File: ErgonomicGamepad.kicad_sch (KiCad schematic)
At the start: 86 parts, among them J1 USB_C_Receptacle_USB2.0_16P, J2 Conn_01x05, J3 Conn_01x05, J4 Conn_01x05, J5 AVR-ISP-6, J6 Conn_01x05, J7 1824417, SW01 SW_DIP_x01, SW02 SW_DIP_x01, SW03 SW_DIP_x01, SW04 SW_DIP_x01, SW05 SW_DIP_x01, SW06 SW_DIP_x01, SW07 SW_DIP_x01, SW08 SW_DIP_x01, SW09 SW_DIP_x01, SW10 SW_DIP_x01, SW11 SW_DIP_x01, SW12 SW_DIP_x01, SW13 SW_DIP_x01, SW14 SW_DIP_x01, SW15 SW_DIP_x01, SW16 SW_DIP_x01, SW17 SW_DIP_x01, SW18 SW_DIP_x01, SW19 SW_DIP_x01, SW20 SW_DIP_x01, SW21 SW_DIP_x01, SW22 SW_DIP_x01, SW23 SW_DIP_x01, SW24 SW_DIP_x01, U1 ATmega32U4-A, U2 USBLC6-2SC6, Y1 Crystal

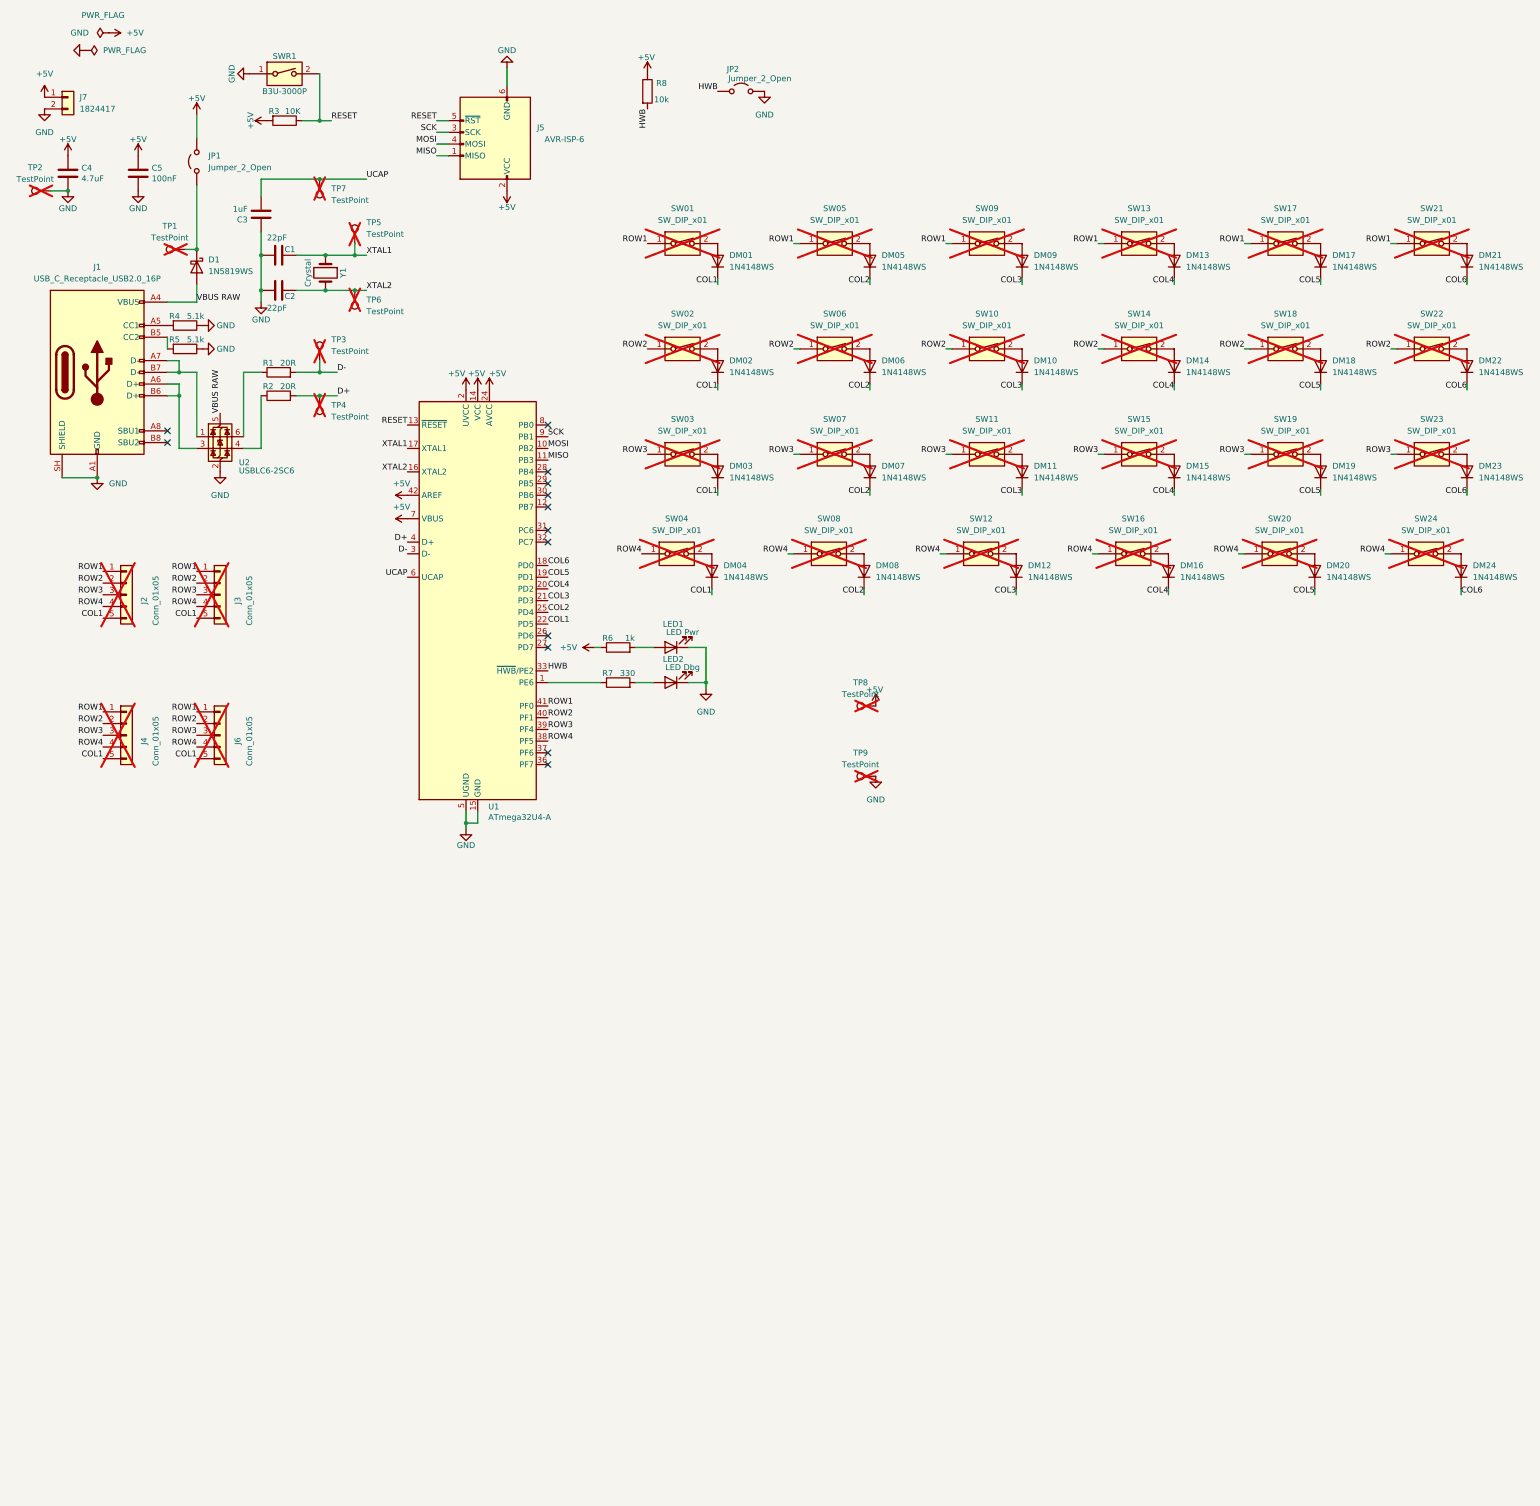
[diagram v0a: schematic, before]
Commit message: Split key matrix into Pinkie/Thumb satellite hierarchical sheets
Move satellite switches off the main schematic into their own sheets
and promote the crossing ROW/COL matrix nets to global labels so
connectivity survives the sheet boundary.
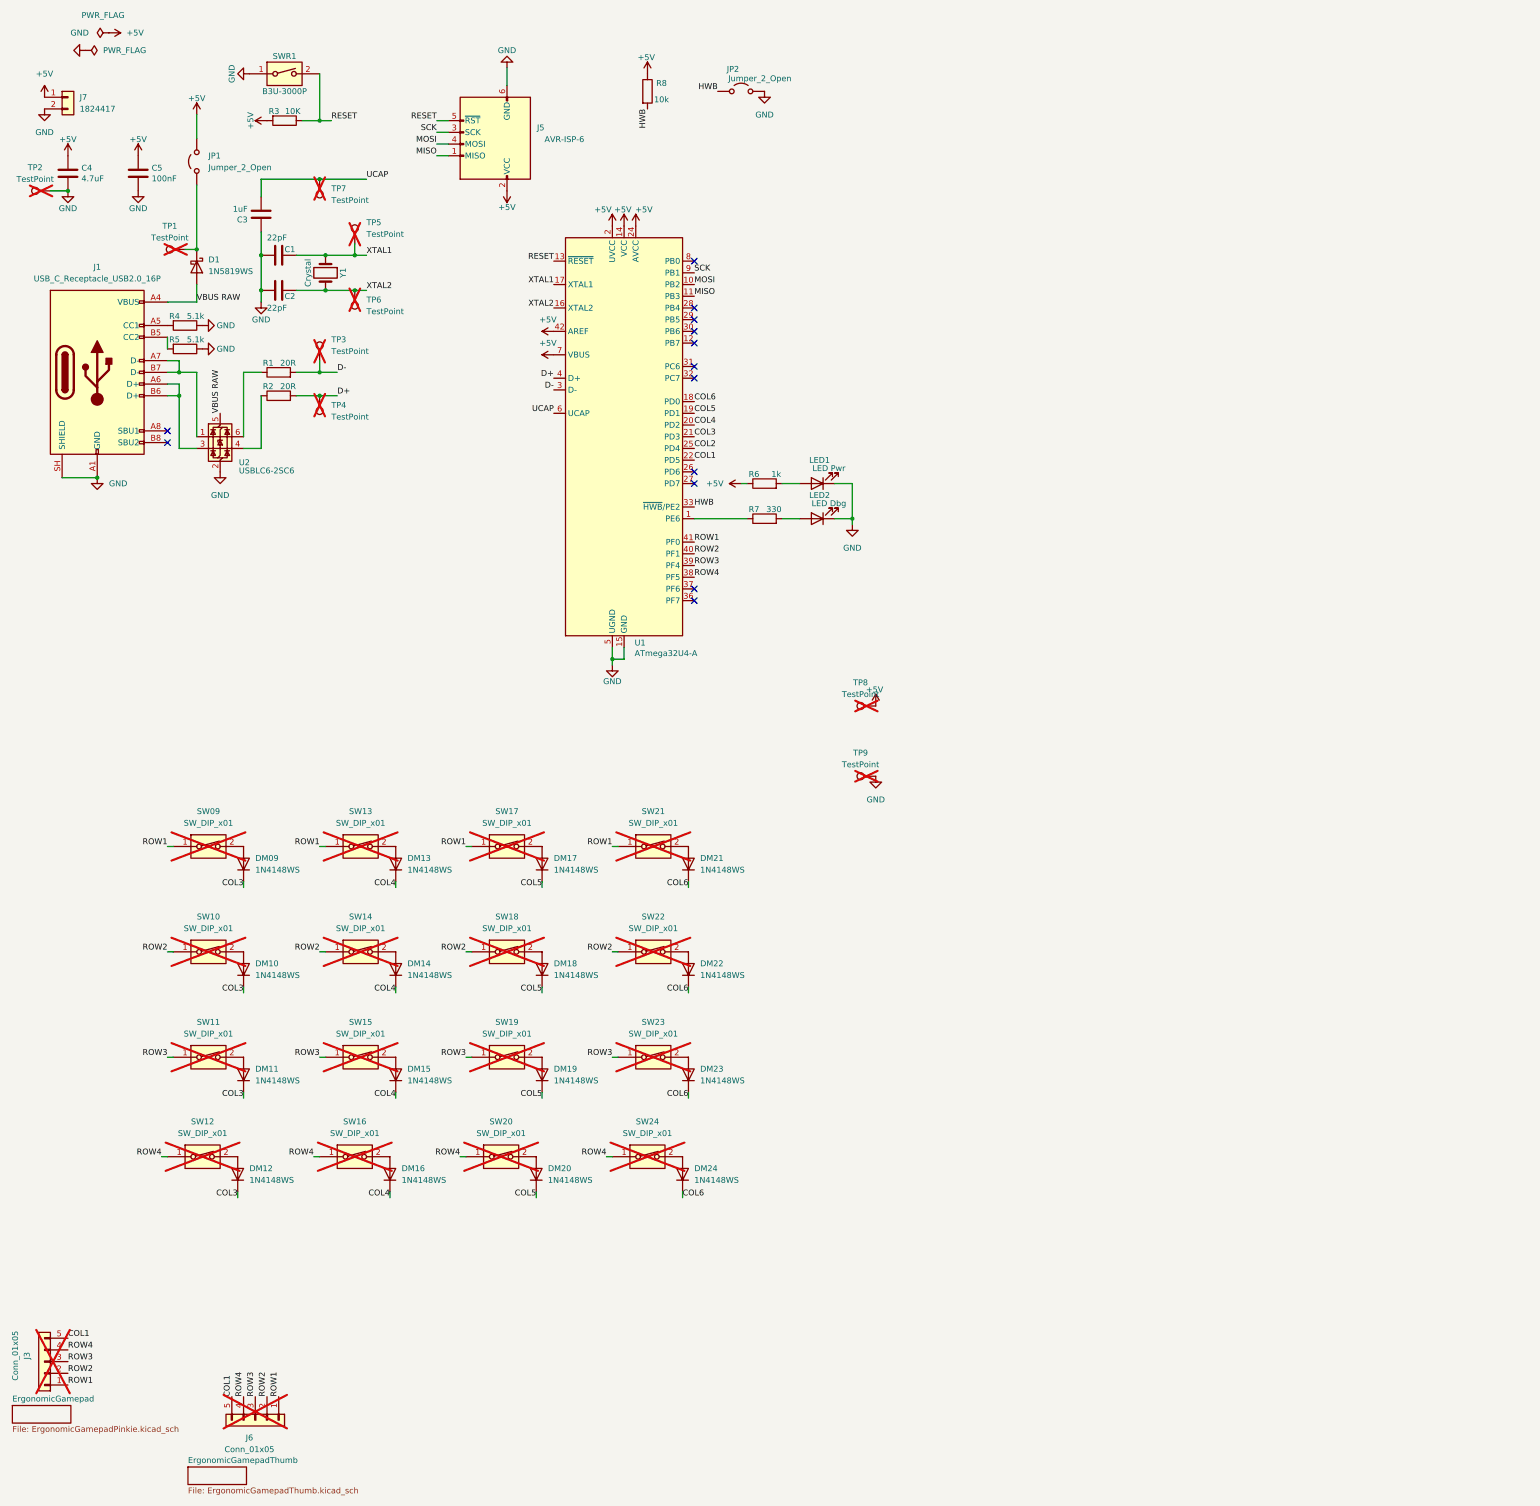
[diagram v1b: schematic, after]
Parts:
- removed DM01, DM02, DM03, DM04, DM05, DM06, DM07, DM08: 1N4148WS, Diode_SMD:D_SOD-323, symbol Device:D
- removed J2, J4: Conn_01x05, Connector_JST:JST_XH_B5B-XH-A_1x05_P2.50mm_Vertical, symbol Connector_Generic:Conn_01x05
- removed SW01, SW02, SW03, SW04, SW05, SW06, SW07, SW08: SW_DIP_x01, Switch_Keyboard_Hotswap_Kailh:SW_Hotswap_Kailh_MX_Plated_1.00u, symbol Switch:SW_DIP_x01
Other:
- added sheet ErgonomicGamepad (ErgonomicGamepadPinkie.kicad_sch)
- added sheet ErgonomicGamepadThumb (ErgonomicGamepadThumb.kicad_sch)
- moved on the sheet: DM09, DM10, DM11, DM12, DM13, DM14, DM15, DM16, DM17, DM18, DM19, DM20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

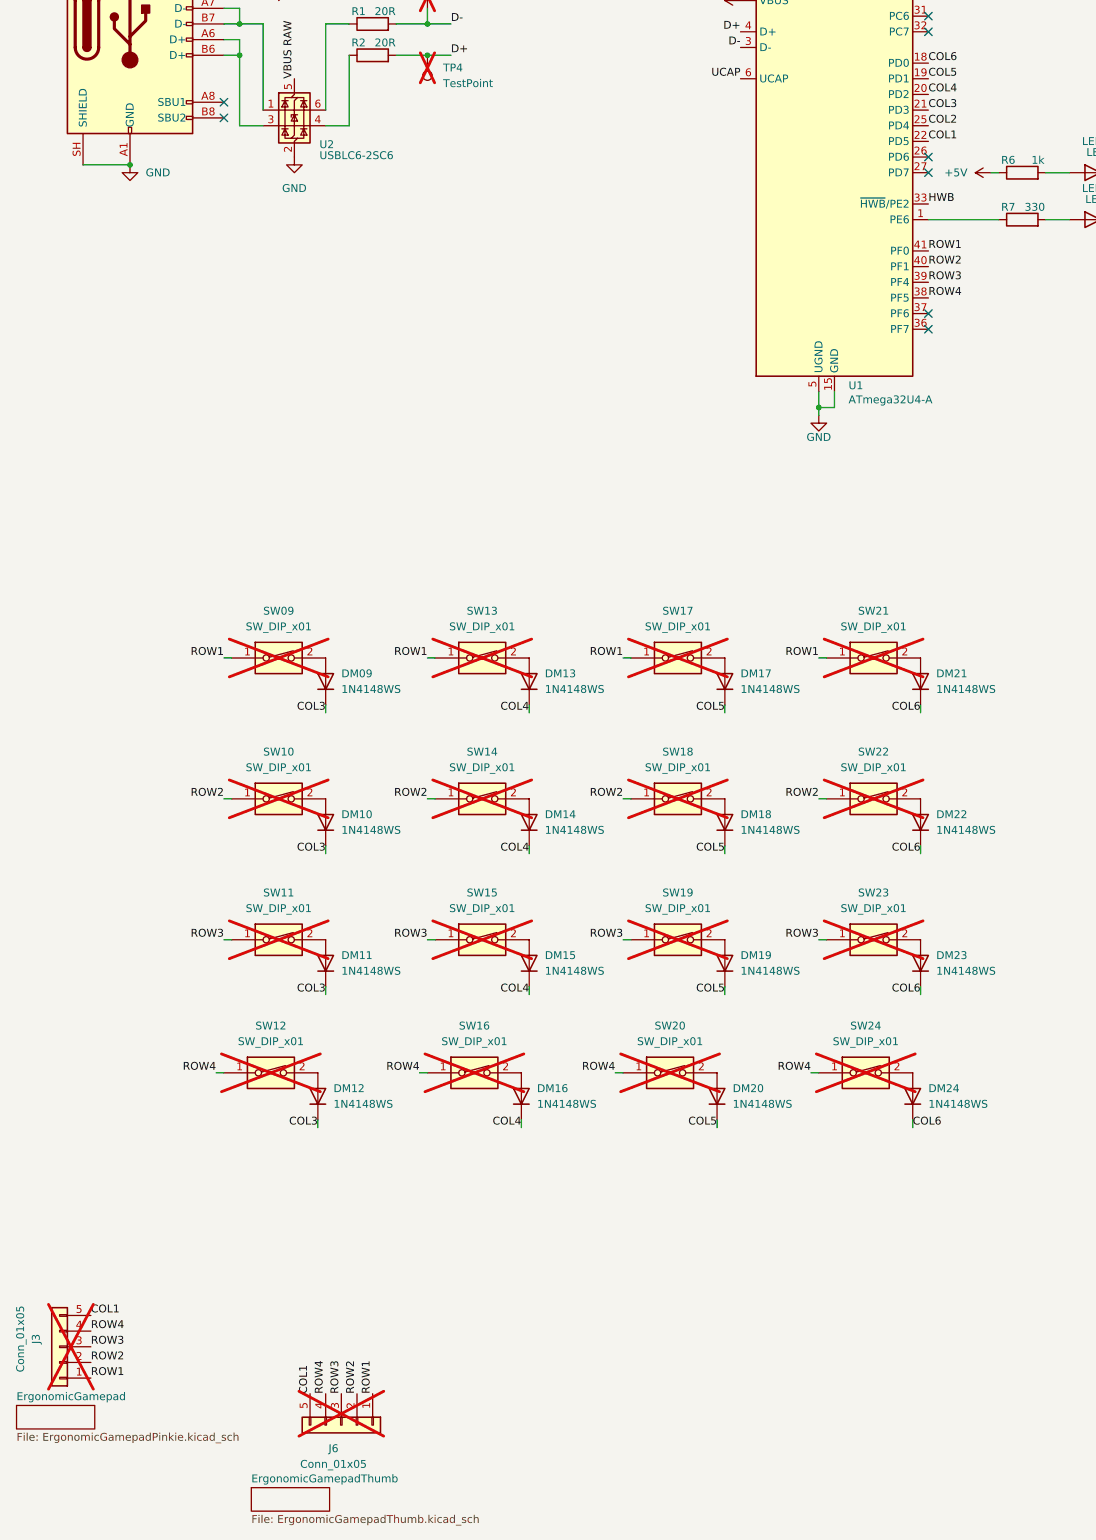
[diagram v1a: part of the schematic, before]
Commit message: Continue ergonomic key stagger adjustments across satellite sheets
Update the layout-mirror script to read symbol positions from every
kicad_sch in the project, since the key matrix now lives across the
Pinkie/Thumb satellite sheets rather than a single top-level sheet.
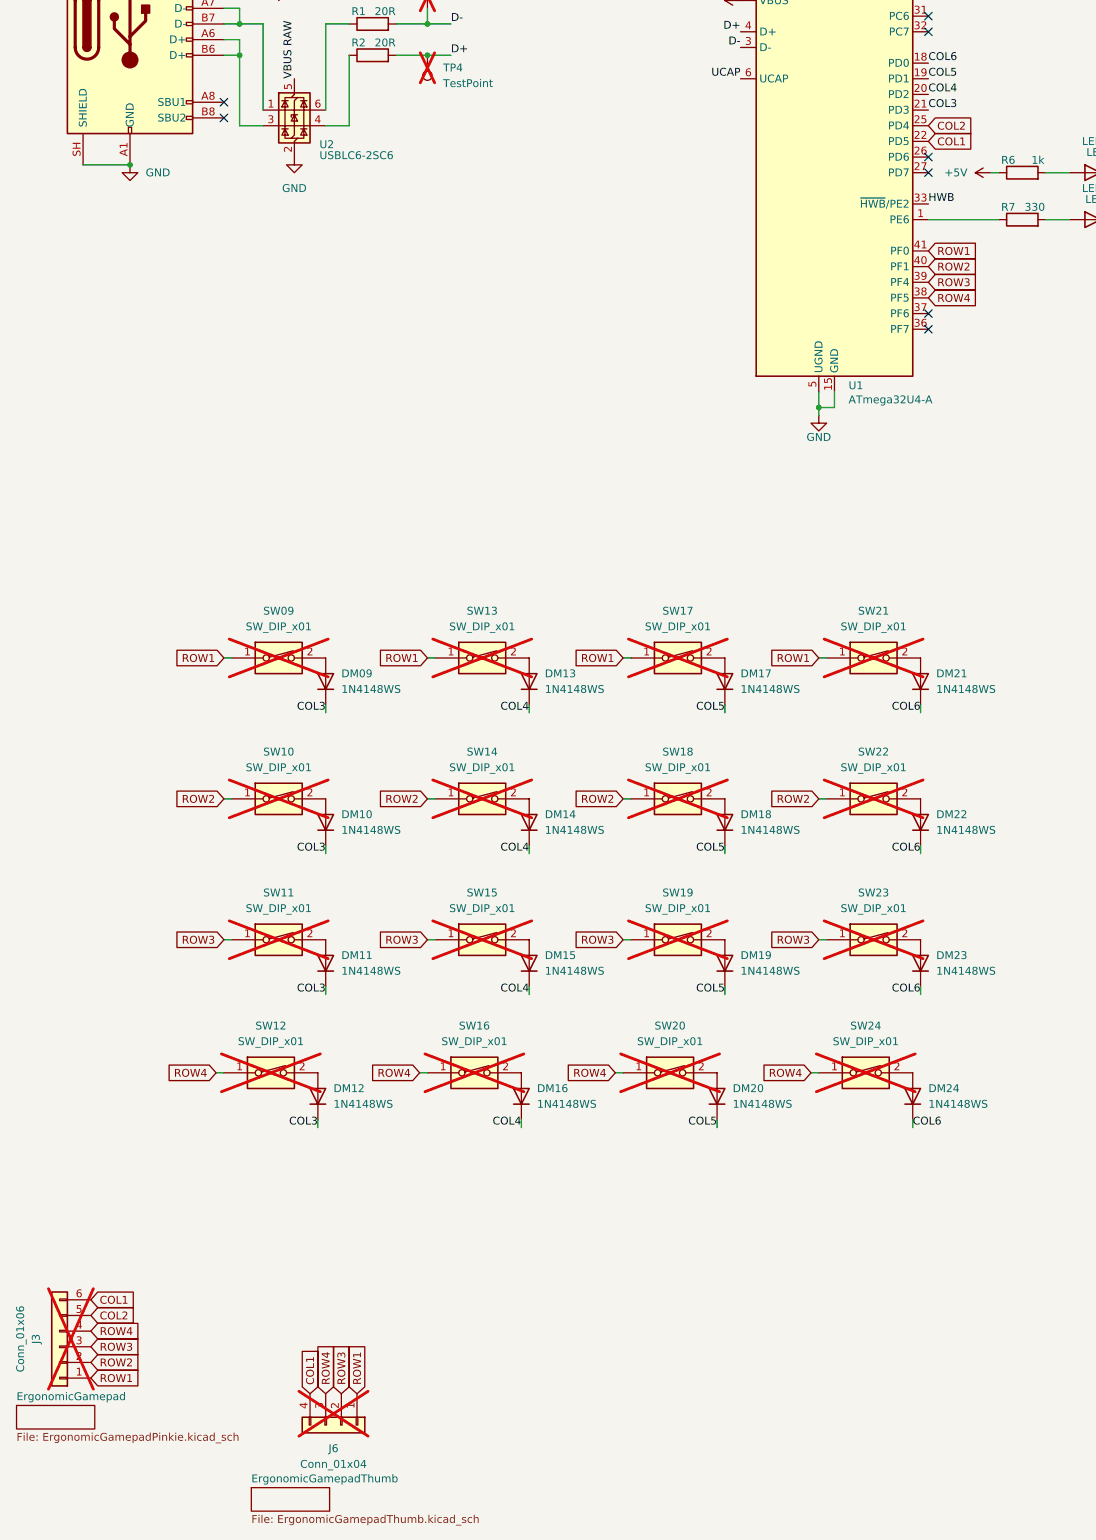
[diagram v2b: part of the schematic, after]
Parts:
- J3: value Conn_01x05 -> Conn_01x06; footprint Connector_JST:JST_XH_B5B-XH-A_1x05_P2.50mm_Vertical -> Connector_JST:JST_XH_B6B-XH-A_1x06_P2.50mm_Vertical; symbol Connector_Generic:Conn_01x05 -> Connector_Generic:Conn_01x06; LCSC C157991 -> C144397; MPN B5B-XH-A(LF)(SN) -> B6B-XH-A(LF)(SN)
- J6: value Conn_01x05 -> Conn_01x04; footprint Connector_JST:JST_XH_B5B-XH-A_1x05_P2.50mm_Vertical -> Connector_JST:JST_XH_B4B-XH-A_1x04_P2.50mm_Vertical; symbol Connector_Generic:Conn_01x05 -> Connector_Generic:Conn_01x04; LCSC C157991 -> C144395; MPN B5B-XH-A(LF)(SN) -> B4B-XH-A(LF)(SN)
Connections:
- net COL1: now also J3.6 (Pin_6), J6.4 (Pin_4); no longer J3.5 (Pin_5), J6.5 (Pin_5)
- net COL2: now also J3.5 (Pin_5)
- net ROW2: no longer J6.2 (Pin_2)
- net ROW3: now also J6.2 (Pin_2); no longer J6.3 (Pin_3)
- net ROW4: now also J6.3 (Pin_3); no longer J6.4 (Pin_4)
